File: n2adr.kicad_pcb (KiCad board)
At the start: 4 copper layers, 100 x 50 mm, 106 parts, among them CN1 STEREO, CN2 Conn_01x20, CN3 SMA, CN4 SMA, CN5 SMA, CN6 SMA, CN7 SMA, CN8 SMA, J1 coax rf low, J2 coax rx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

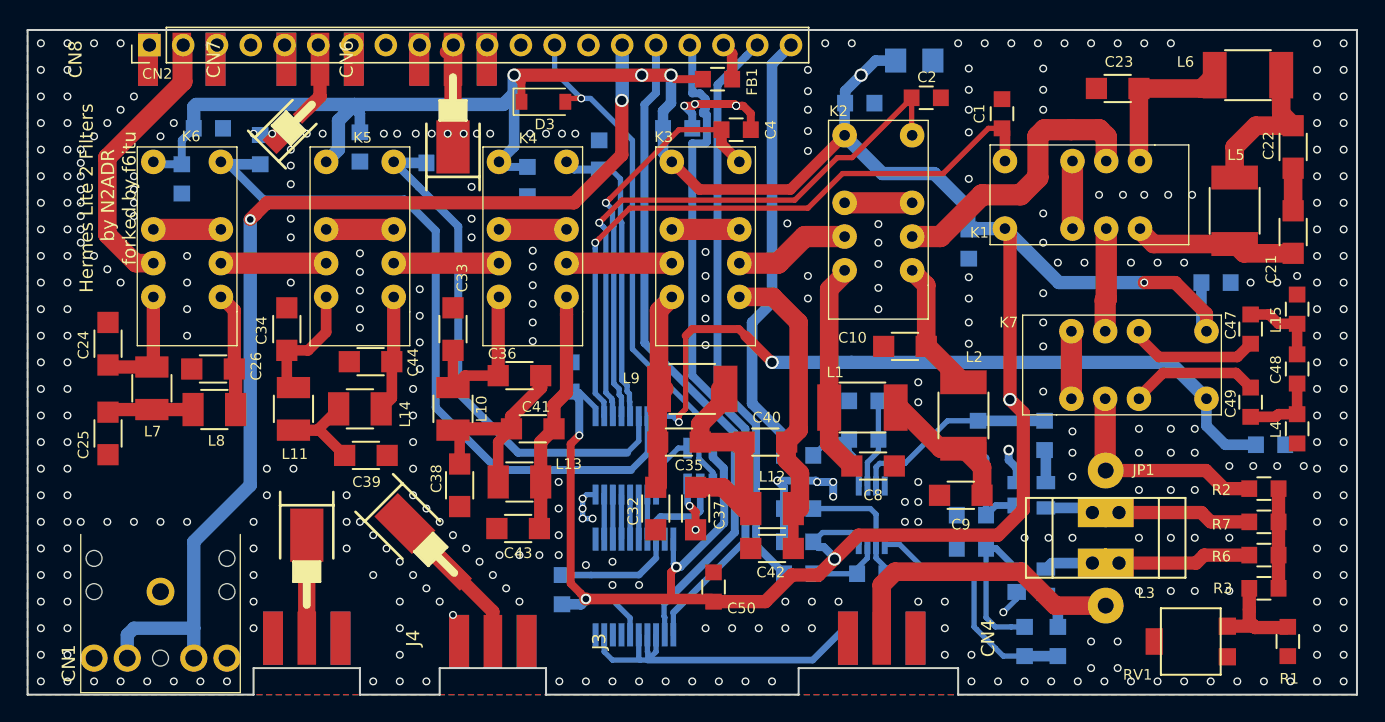
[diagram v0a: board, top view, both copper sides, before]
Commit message: upgrade to Kicad 5.x, 2 layers less
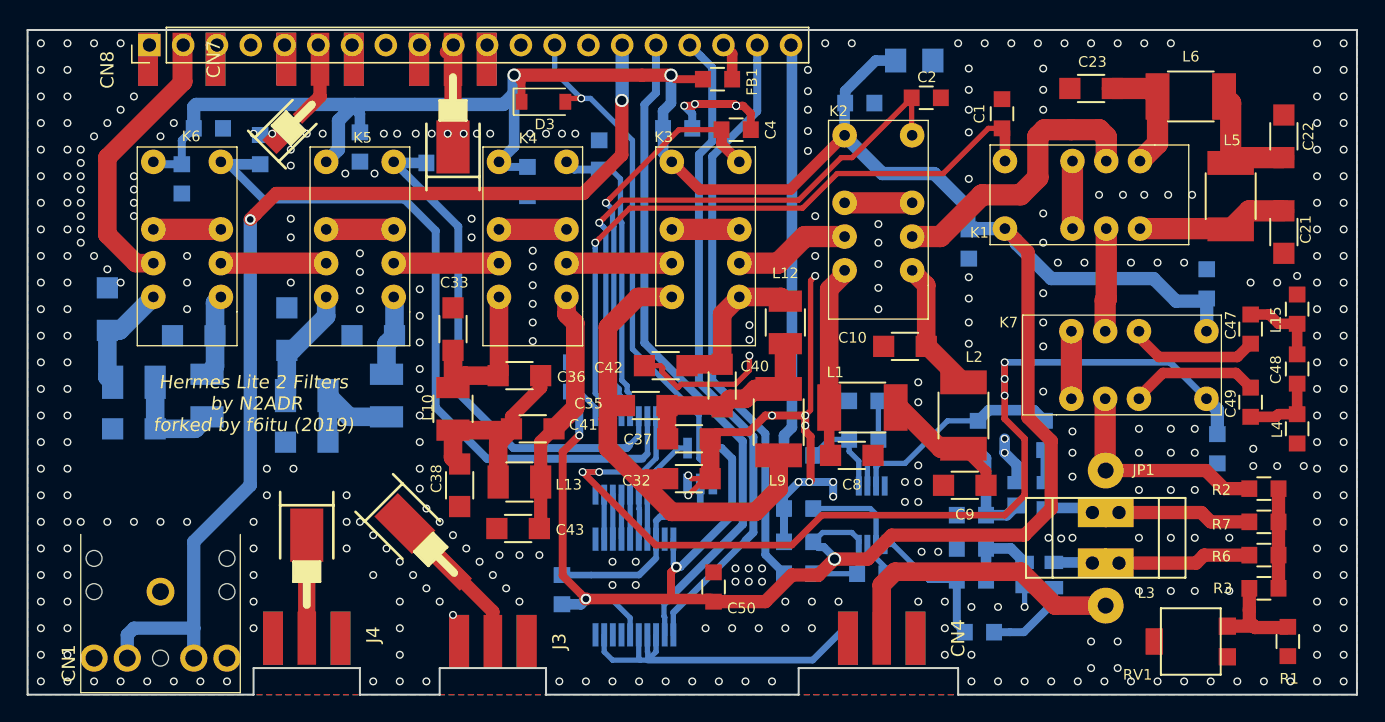
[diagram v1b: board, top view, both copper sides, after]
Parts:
- C24, C25, C26, C34, C39, C44, L11, L14, L7, L8: moved to B.Cu
- moved C42 15.9 mm to (113.0, 80.2)
- moved L12 14.0 mm to (122.0, 77.0), turned to 90 degrees
- moved L9 6.96 mm to (121.5, 84.5), turned to 90 degrees
- moved R5 6.10 mm to (136.0, 96.4), turned to 0 degrees
- moved R4 5.94 mm to (136.6, 100.3), turned to 0 degrees
- moved C40 5.35 mm to (117.2, 81.8), turned to 270 degrees
- moved C37 5.27 mm to (114.8, 85.8), turned to 180 degrees
- moved L6 4.59 mm to (152.5, 60.0)
- moved C39 4.56 mm to (86.0, 86.0), turned to 0 degrees
- moved C46 4.01 mm to (154.5, 86.5), turned to 90 degrees
- moved C35 3.72 mm to (111.5, 83.2)
- moved C32 3.36 mm to (114.8, 88.8), turned to 180 degrees
- moved C26 2.89 mm to (77.5, 78.0)
- moved C24 2.60 mm to (71.0, 76.0)
- moved L14 2.24 mm to (92.0, 82.5), turned to 90 degrees
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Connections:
- RV1 pad 3: (no net) -> GND
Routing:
- net GND: track 60.3 -> 91.2 mm, vias 378 -> 380
- net Net-(C32-Pad2): track 15.1 -> 38.8 mm
- net Band7: track 56.5 -> 79.6 mm, vias 2 -> 5
- net Net-(C40-Pad1): track 23.1 -> 11.9 mm
- net Net-(R4-Pad1): track 18.7 -> 10.7 mm
- net Net-(C11-Pad1): track 11.6 -> 6.04 mm
- net Net-(D1-Pad4): track 2.82 -> 6.53 mm
- net Net-(C44-Pad2): track 8.81 -> 6.09 mm
- net Net-(C23-Pad1): track 11.7 -> 9.06 mm
- net Net-(C26-Pad2): track 8.93 -> 6.31 mm
- net Net-(C22-Pad1): track 11.5 -> 9.37 mm
- net Net-(C35-Pad1): track 17.2 -> 15.1 mm
- net +3V3: track 243.2 -> 245.2 mm, vias 10 -> 6
- net Net-(CN2-Pad20): track 33.1 -> 31.2 mm
- net Net-(C8-Pad2): track 16.0 -> 14.6 mm
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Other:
- board text added: "Hermes Lite 2 Filters by N2ADR forked by f6itu (2019)"

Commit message: minor pcb changes still under dev
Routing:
- net Net-(CN2-Pad10): track 0.75 -> 0.00 mm
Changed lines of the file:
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@@
     (thickness 1.6)
     (drawings 28)
-    (tracks 1011)
+    (tracks 1008)
     (zones 0)
     (modules 106)
@@
   )
   (layers
-    (0 F.Cu signal hide)
+    (0 F.Cu signal)
     (1 In1.Cu signal hide)
     (2 In2.Cu signal hide)
@@
   (via (at 122 100) (size 0.6) (drill 0.4) (layers F.Cu B.Cu) (net 1))
   (via (at 124 100) (size 0.6) (drill 0.4) (layers F.Cu B.Cu) (net 1))
-  (via (at 122 98) (size 0.6) (drill 0.4) (layers F.Cu B.Cu) (net 1))
+  (via (at 124 99) (size 0.6) (drill 0.4) (layers F.Cu B.Cu) (net 1))
   (via (at 124 98) (size 0.6) (drill 0.4) (layers F.Cu B.Cu) (net 1))
   (via (at 126 98) (size 0.6) (drill 0.4) (layers F.Cu B.Cu) (net 1))
@@
   (segment (start 115.54 67) (end 122.38 67) (width 0.8) (layer F.Cu) (net 68))
   (segment (start 113.46 64.92) (end 115.54 67) (width 0.8) (layer F.Cu) (net 68) (status 10))
-  (segment (start 125.7 94.8) (end 124.5 96) (width 1) (layer F.Cu) (net 68))
-  (segment (start 124.5 96) (end 122.5 96) (width 1) (layer F.Cu) (net 68))
-  (segment (start 122.5 96) (end 120.5 98) (width 1) (layer F.Cu) (net 68))
   (via (at 106.5 85.5) (size 0.6) (drill 0.4) (layers F.Cu B.Cu) (net 68))
   (segment (start 106.5 82.8) (end 105.9 82.2) (width 0.6) (layer B.Cu) (net 68) (status 30))
   (segment (start 106.5 85.5) (end 106.5 82.8) (width 0.6) (layer B.Cu) (net 68) (status 20))
-  (segment (start 120.5 98) (end 116.6 98) (width 1) (layer F.Cu) (net 68) (status 20))
   (segment (start 113.400001 97.649999) (end 113.25 97.8) (width 0.6) (layer F.Cu) (net 68))
   (segment (start 113.400001 95.799999) (end 113.400001 97.649999) (width 0.6) (layer F.Cu) (net 68))
@@
   (segment (start 153.5 75.4) (end 151.4 75.4) (width 1) (layer B.Cu) (net 68))
   (segment (start 139.38 71.08) (end 139.38 70.8) (width 1) (layer B.Cu) (net 68))
-  (segment (start 130 93) (end 128.2 94.8) (width 1) (layer F.Cu) (net 68))
+  (segment (start 114.1 95.4) (end 113.8 95.4) (width 0.6) (layer B.Cu) (net 68))
+  (segment (start 118 91.5) (end 114.1 95.4) (width 0.6) (layer B.Cu) (net 68))
+  (segment (start 118 87.25) (end 118 91.5) (width 0.6) (layer B.Cu) (net 68))
+  (segment (start 116.55 86.45) (end 117.2 86.45) (width 0.6) (layer B.Cu) (net 68))
+  (segment (start 117.2 86.45) (end 118 87.25) (width 0.6) (layer B.Cu) (net 68))
+  (segment (start 126.5 94) (end 125.7 94.8) (width 1) (layer F.Cu) (net 68))
+  (segment (start 127.5 93) (end 126.5 94) (width 1) (layer F.Cu) (net 68))
   (segment (start 140.25 71.67) (end 140.25 84.15) (width 1) (layer F.Cu) (net 68))
   (segment (start 138.52 69.94) (end 140.25 71.67) (width 1) (layer F.Cu) (net 68))
   (segment (start 140.25 84.15) (end 142 85.9) (width 1) (layer F.Cu) (net 68))
-  (segment (start 128.2 94.8) (end 125.7 94.8) (width 1) (layer F.Cu) (net 68))
   (segment (start 142 85.9) (end 142 91) (width 1) (layer F.Cu) (net 68))
   (segment (start 142 91) (end 140 93) (width 1) (layer F.Cu) (net 68))
-  (segment (start 140 93) (end 130 93) (width 1) (layer F.Cu) (net 68))
-  (segment (start 105.25 96.05) (end 106.600001 97.400001) (width 0.6) (layer F.Cu) (net 68))
+  (segment (start 140 93) (end 127.5 93) (width 1) (layer F.Cu) (net 68))
+  (segment (start 122.5 98) (end 116.6 98) (width 1) (layer F.Cu) (net 68))
+  (segment (start 125.7 94.8) (end 122.5 98) (width 1) (layer F.Cu) (net 68))
   (segment (start 106.600001 97.400001) (end 107 97.8) (width 0.6) (layer F.Cu) (net 68))
-  (segment (start 105.25 86.75) (end 105.25 96.05) (width 0.6) (layer F.Cu) (net 68))
-  (segment (start 106.5 85.5) (end 105.25 86.75) (width 0.6) (layer F.Cu) (net 68))
-  (segment (start 114.1 95.4) (end 113.8 95.4) (width 0.6) (layer B.Cu) (net 68))
-  (segment (start 118 91.5) (end 114.1 95.4) (width 0.6) (layer B.Cu) (net 68))
-  (segment (start 118 87.25) (end 118 91.5) (width 0.6) (layer B.Cu) (net 68))
-  (segment (start 116.55 86.45) (end 117.2 86.45) (width 0.6) (layer B.Cu) (net 68))
-  (segment (start 117.2 86.45) (end 118 87.25) (width 0.6) (layer B.Cu) (net 68))
+  (segment (start 105.5 96.3) (end 106.600001 97.400001) (width 0.6) (layer F.Cu) (net 68))
+  (segment (start 106.5 85.5) (end 105.5 86.5) (width 0.6) (layer F.Cu) (net 68))
+  (segment (start 105.5 86.5) (end 105.5 96.3) (width 0.6) (layer F.Cu) (net 68))
   (segment (start 105.2 96) (end 107.4 96) (width 0.5) (layer B.Cu) (net 69) (status 10))
   (segment (start 112.275 94.725) (end 111 96) (width 0.5) (layer B.Cu) (net 69))
@@
   (segment (start 87 60) (end 86.002082 60.997918) (width 1) (layer F.Cu) (net 70))
   (segment (start 87 57.2) (end 87 60) (width 1) (layer F.Cu) (net 70))
-  (segment (start 96.5 56.662) (end 97.028 56.134) (width 1) (layer F.Cu) (net 71) (status 30))
   (segment (start 112.87499 99.114954) (end 112.925 99.164964) (width 0.4) (layer B.Cu) (net 72))
   (segment (start 112.925 99.164964) (end 112.925 99.225) (width 0.4) (layer B.Cu) (net 72))
